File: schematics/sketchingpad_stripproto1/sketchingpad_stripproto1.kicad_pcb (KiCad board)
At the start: 4 copper layers, 160 x 59.6 mm, 73 parts, among them CN1 HC-1.0-4PWT, CN2 S2B-PH-SM4-TB, J1 Conn_01x07, J2 Conn_01x07, J3 Conn_01x03, SW1 TS-1088-AR02016, U1 TS20

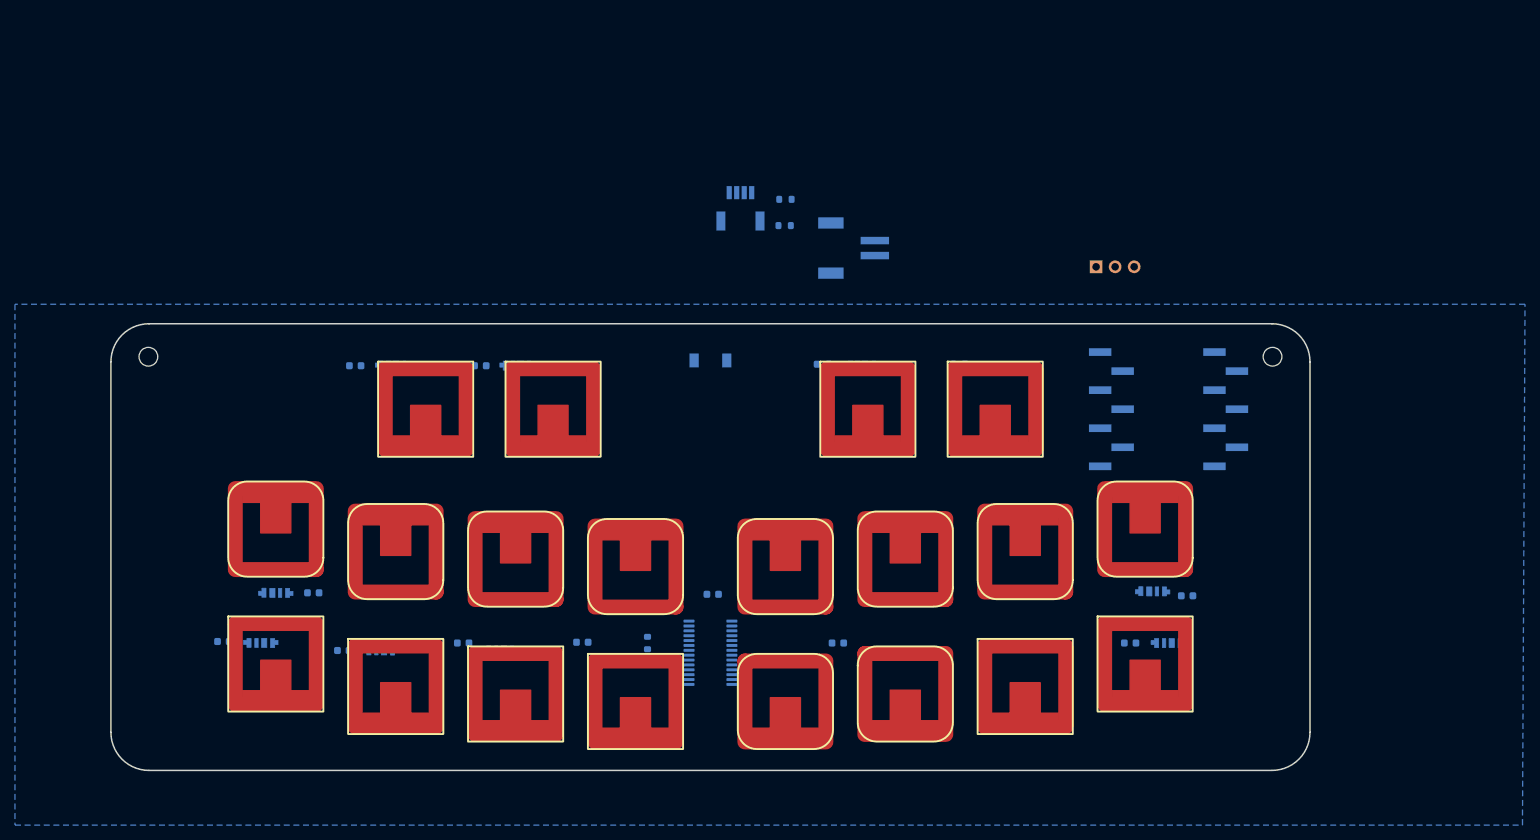
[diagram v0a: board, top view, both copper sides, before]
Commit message: add arduino hwtest
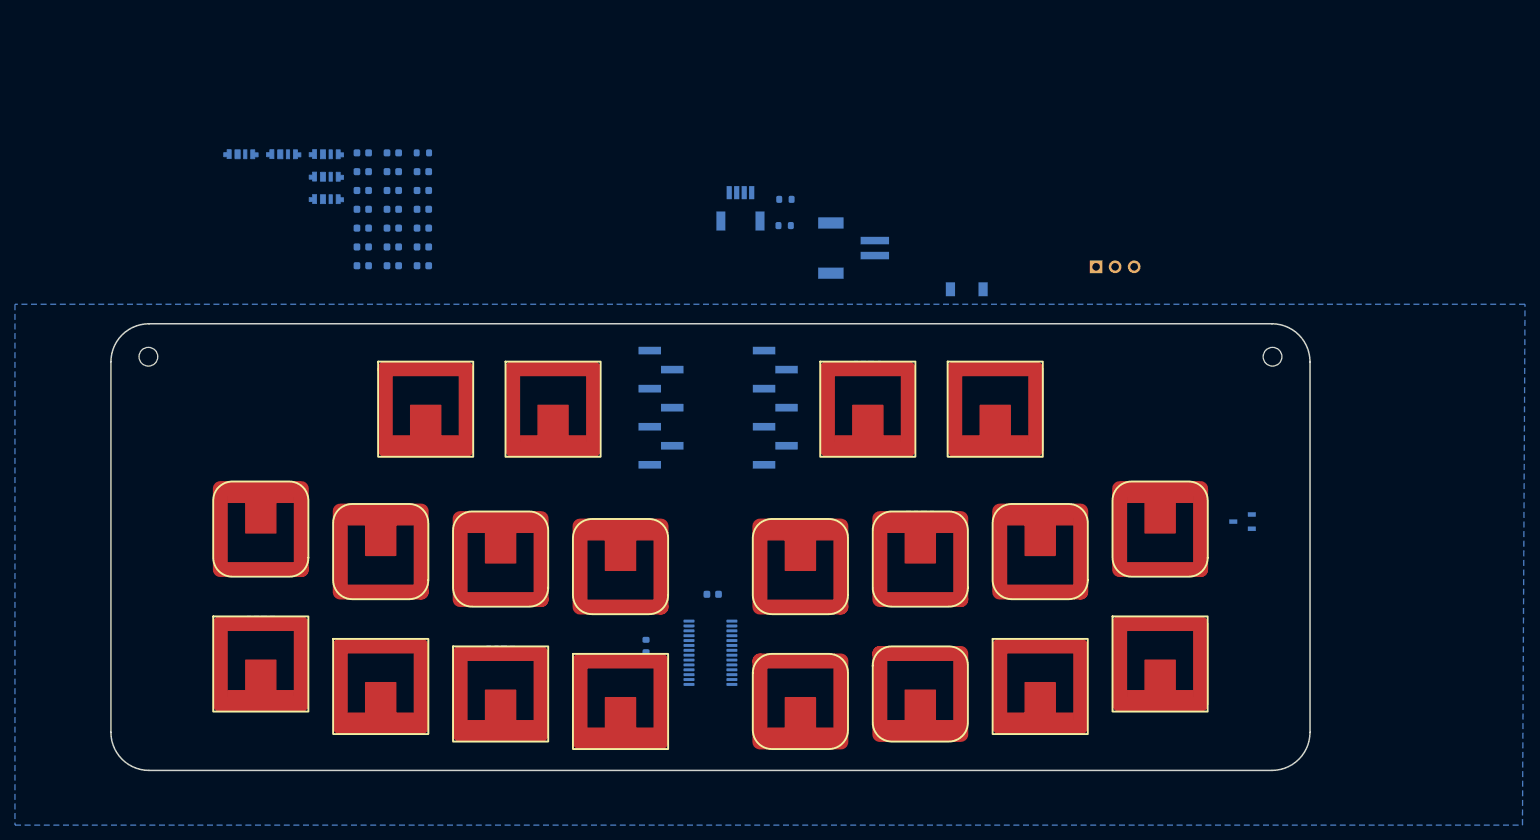
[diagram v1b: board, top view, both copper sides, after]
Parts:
- added Q1: AO3415A, easyeda2kicad:SOT-23-3_L2.9-W1.6-P1.90-LS2.8-BR, B.Cu at (207.0, 122.0)
- added R19: 100k, Resistor_SMD:R_0603_1608Metric, B.Cu at (97.6, 72.8)
- moved LED16 129.9 mm to (84.8, 73.0), turned to 0 degrees
- moved LED8 123.4 mm to (84.8, 76.0)
- moved C8 115.4 mm to (97.6, 77.8), turned to 0 degrees
- moved C16 113.4 mm to (97.6, 75.3)
- moved LED15 112.2 mm to (84.8, 79.0), turned to 0 degrees
- moved C7 98.1 mm to (97.6, 82.8), turned to 0 degrees
- moved C15 96.6 mm to (97.6, 80.3)
- moved LED5 90.1 mm to (79.0, 73.0)
- moved C13 88.3 mm to (93.6, 72.8)
- moved C6 82.1 mm to (97.6, 87.9), turned to 0 degrees
- moved C14 81.7 mm to (97.6, 85.3)
- moved C5 81.2 mm to (93.6, 75.3), turned to 0 degrees
- moved C20 77.7 mm to (93.6, 82.8)
- moved C19 67.6 mm to (89.6, 72.8)
- moved C12 65.4 mm to (93.6, 77.8), turned to 0 degrees
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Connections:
- net /Root/SCL renamed /SCL
- net /Root/SDA renamed /SDA
- net /Root/TOUCH1 renamed /TOUCH1
- net /Root/TOUCH10 renamed /TOUCH10
- net /Root/TOUCH11 renamed /TOUCH11
- net /Root/TOUCH12 renamed /TOUCH12
- net /Root/TOUCH13 renamed /TOUCH13
- net /Root/TOUCH14 renamed /TOUCH14
- net /Root/TOUCH15 renamed /TOUCH15
- net /Root/TOUCH16 renamed /TOUCH16
- net /Root/TOUCH17 renamed /TOUCH17
- net /Root/TOUCH18 renamed /TOUCH18
- net /Root/TOUCH19 renamed /TOUCH19
- net /Root/TOUCH2 renamed /TOUCH2
- net /Root/TOUCH20 renamed /TOUCH20
- net /Root/TOUCH3 renamed /TOUCH3
- net /Root/TOUCH4 renamed /TOUCH4
- net /Root/TOUCH5 renamed /TOUCH5
- net /Root/TOUCH6 renamed /TOUCH6
- net /Root/TOUCH7 renamed /TOUCH7
- net /Root/TOUCH8 renamed /TOUCH8
- net /Root/TOUCH9 renamed /TOUCH9
- net LED_DAT renamed /LED_DAT
- C1 pad 1: +3.3V -> 3V3_LED
- C10 pad 1: +3.3V -> 3V3_LED
- C11 pad 1: +3.3V -> 3V3_LED
- C12 pad 1: +3.3V -> 3V3_LED
- C13 pad 1: +3.3V -> 3V3_LED
- C14 pad 1: +3.3V -> 3V3_LED
- C15 pad 1: +3.3V -> 3V3_LED
- C16 pad 1: +3.3V -> 3V3_LED
- C17 pad 1: +3.3V -> 3V3_LED
- C18 pad 1: +3.3V -> 3V3_LED
- C19 pad 1: +3.3V -> 3V3_LED
- C2 pad 1: +3.3V -> 3V3_LED
- C20 pad 1: +3.3V -> 3V3_LED
- C3 pad 1: +3.3V -> 3V3_LED
- C4 pad 1: +3.3V -> 3V3_LED
- C5 pad 1: +3.3V -> 3V3_LED
- C6 pad 1: +3.3V -> 3V3_LED
- C7 pad 1: +3.3V -> 3V3_LED
- C8 pad 1: +3.3V -> 3V3_LED
- C9 pad 1: +3.3V -> 3V3_LED
- CN2 pad 2: unconnected-(CN2-Pad2) -> /VBAT
- J1 pad 3: unconnected-(J1-Pin_3-Pad3) -> /BUTTON
- J1 pad 4: unconnected-(J1-Pin_4-Pad4) -> /TS20_INT
- J2 pad 7: unconnected-(J2-Pin_7-Pad7) -> /LED_POWER
- J3 pad 1: /Root/VBAT -> /VBAT
- LED1 pad 2: +3.3V -> 3V3_LED
- LED10 pad 2: +3.3V -> 3V3_LED
- LED11 pad 2: +3.3V -> 3V3_LED
- LED12 pad 2: +3.3V -> 3V3_LED
- LED13 pad 2: +3.3V -> 3V3_LED
- LED14 pad 2: +3.3V -> 3V3_LED
- LED15 pad 2: +3.3V -> 3V3_LED
- LED16 pad 2: +3.3V -> 3V3_LED
- LED17 pad 2: +3.3V -> 3V3_LED
- LED18 pad 2: +3.3V -> 3V3_LED
- LED19 pad 2: +3.3V -> 3V3_LED
- LED2 pad 2: +3.3V -> 3V3_LED
- LED20 pad 2: +3.3V -> 3V3_LED
- LED3 pad 2: +3.3V -> 3V3_LED
- LED4 pad 2: +3.3V -> 3V3_LED
- LED5 pad 2: +3.3V -> 3V3_LED
- LED6 pad 2: +3.3V -> 3V3_LED
- LED7 pad 2: +3.3V -> 3V3_LED
- LED8 pad 2: +3.3V -> 3V3_LED
- LED9 pad 2: +3.3V -> 3V3_LED
- R16 pad 1: Net-(U1-INT) -> /TS20_INT
- SW1 pad 1: unconnected-(SW1-Pad1) -> /BUTTON
- U1 pad 19: Net-(U1-INT) -> /TS20_INT

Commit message: going with SMD-mounted XIAO I guess, added audio. ERC clean
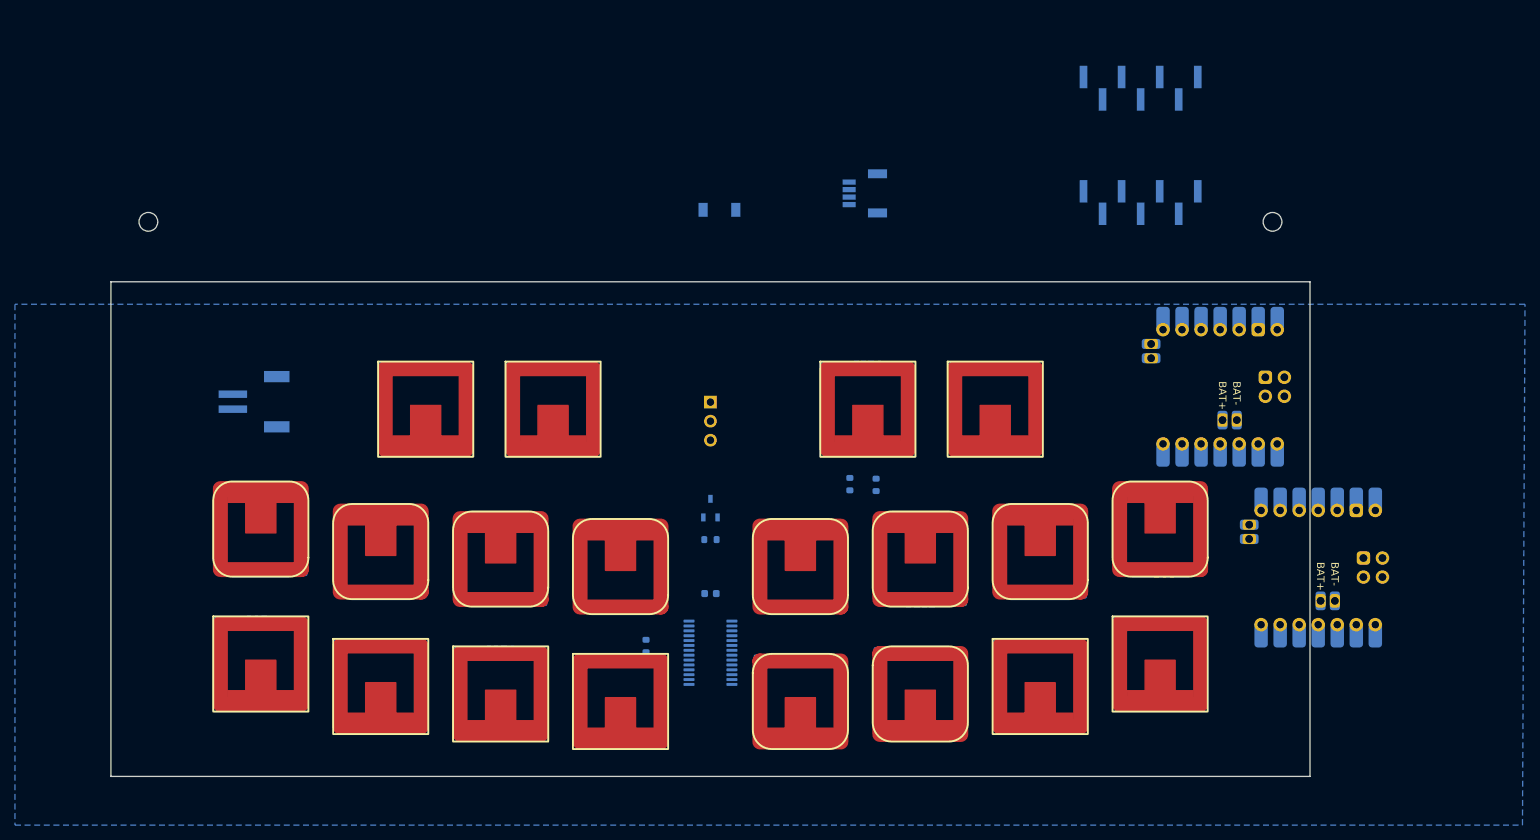
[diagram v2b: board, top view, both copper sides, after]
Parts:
- added U2: Seeeduino Xiao nRF52840, PCM_marbastlib-xp-promicroish:Xiao_nRF52840_ACH, B.Cu at (204.0, 104.0)
- added U3: XIAO-nRF52840-SMD, PCM_marbastlib-xp-promicroish:Xiao_nRF52840_ACH, B.Cu at (217.1, 128.1)
- moved LED16 127.5 mm to (196.0, 135.3), turned to 180 degrees
- moved LED8 123.2 mm to (196.0, 128.8)
- moved C8 115.1 mm to (200.8, 128.8), turned to 180 degrees
- moved LED15 112.2 mm to (180.0, 138.2), turned to 180 degrees
- moved C16 110.9 mm to (191.0, 135.2)
- moved C7 100.2 mm to (185.0, 131.8), turned to 180 degrees
- moved C15 96.6 mm to (175.0, 138.2)
- moved LED5 91.9 mm to (148.0, 133.8)
- moved C6 84.3 mm to (169.0, 132.8), turned to 180 degrees
- moved C13 83.6 mm to (143.0, 140.2)
- moved C5 83.2 mm to (152.8, 133.8), turned to 180 degrees
- moved CN2 82.4 mm to (75.2, 106.0), turned to -90 degrees
- moved C14 81.7 mm to (159.0, 139.2)
- moved C20 77.6 mm to (169.0, 101.2)
- moved J2 76.9 mm to (193.4, 64.2), turned to 180 degrees
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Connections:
- J1 pad 1: unconnected-(J1-Pin_1-Pad1) -> /PWM_AUDIO
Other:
- board size 160 x 59.6 mm -> 160 x 66 mm

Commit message: final on the sketchingpad_stripproto1 sch maybe
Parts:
- removed J1, J2: Conn_01x07, easyeda2kicad:HDR-SMD_7P-P2.54_HX-PM2.54-1X7P-TP-YQ
- removed U3: XIAO-nRF52840-SMD, PCM_marbastlib-xp-promicroish:Xiao_nRF52840_ACH
- added C21: 100n, Capacitor_SMD:C_0603_1608Metric, B.Cu at (77.5, 75.7)
- added C22: 47u, Capacitor_SMD:C_0603_1608Metric, B.Cu at (80.0, 75.7)
- added R21: 220, Resistor_SMD:R_0603_1608Metric, B.Cu at (82.5, 75.7)
- added R22: 100, Resistor_SMD:R_0603_1608Metric, B.Cu at (85.0, 75.7)
- added R23: 1.8k, Resistor_SMD:R_0603_1608Metric, B.Cu at (87.5, 75.7)
- added SW2: MINI MSK12CO2, easyeda2kicad:SW-SMD_MSK12CO2, B.Cu at (188.8, 62.3)
- added TP21: TestPoint, TestPoint:TestPoint_Pad_D1.5mm, B.Cu at (197.4, 76.3)
- added TP22: TestPoint, TestPoint:TestPoint_Pad_D1.5mm, B.Cu at (200.9, 76.3)
- J3: value Conn_01x03 -> AudioJack4; footprint Connector_PinSocket_2.54mm:PinSocket_1x03_P2.54mm_Vertical -> todbot_stuff:Jack_3.5mm_PJ320D_Horizontal
- SW1: value TS-1088-AR02016 -> TC-S3601-3.5-260G-F0.6; footprint easyeda2kicad:SW-SMD_L3.9-W3.0-P4.45 -> easyeda2kicad:SW-SMD_TC-S3601-3.5-260G-F0.6
- U2: footprint PCM_marbastlib-xp-promicroish:Xiao_nRF52840_ACH -> todbot_stuff:Xiao_nRF52840_ACH-todedit
- moved CN2 129.5 mm to (199.0, 68.0), turned to 180 degrees
- moved U2 75.7 mm to (136.0, 70.7), turned to 180 degrees
- moved J3 68.0 mm to (80.2, 67.2), turned to -90 degrees
- moved R19 41.6 mm to (128.5, 83.5)
- moved SW1 35.8 mm to (106.4, 62.1), turned to 180 degrees
- moved Q1 34.1 mm to (128.4, 87.0), turned to 90 degrees
- moved C1 31.0 mm to (81.0, 97.8)
- moved C2 31.0 mm to (96.8, 100.8)
- moved C3 31.0 mm to (113.0, 101.8)
- moved C4 31.0 mm to (128.8, 102.8)
- moved C5 31.0 mm to (152.8, 102.8)
- moved C6 31.0 mm to (169.0, 101.8)
- moved C7 31.0 mm to (185.0, 100.8)
- moved C8 31.0 mm to (200.8, 97.8)
- moved LED1 31.0 mm to (76.0, 97.7)
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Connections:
- CN2 pad 2: /VBAT -> Net-(CN2-Pad2)
- LED1 pad 1: /LED_DAT -> /LED_DATA
- U2 pad 1: unconnected-(U2-P0.02-Pad1) -> /PWM_AUDIO
- U2 pad 10: unconnected-(U2-3V3-Pad10) -> +3.3V
- U2 pad 11: unconnected-(U2-P1.15-Pad11) -> /BUTTON
- U2 pad 14: unconnected-(U2-P1.12-Pad14) -> /LED_POWER
- U2 pad 15: unconnected-(U2-BAT--Pad15) -> GND
- U2 pad 16: unconnected-(U2-BAT+-Pad16) -> /VBAT
- U2 pad 4: unconnected-(U2-P0.29-Pad4) -> /TS20_INT
- U2 pad 5: unconnected-(U2-P0.04-Pad5) -> /SDA
- U2 pad 6: unconnected-(U2-P0.05-Pad6) -> /SCL
- U2 pad 7: unconnected-(U2-P1.11-Pad7) -> /LED_DATA
- U2 pad 9: unconnected-(U2-GND-Pad9) -> GND
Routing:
- net /VBAT: track 0.00 -> 63.6 mm, vias 0 -> 1
- net /PWM_AUDIO: track 0.00 -> 63.6 mm
- net /SDA: track 0.00 -> 45.8 mm, vias 0 -> 2
- net /TS20_INT: track 0.00 -> 45.5 mm, vias 0 -> 1
- net /SCL: track 0.00 -> 45.0 mm, vias 0 -> 2
- net /BUTTON: track 0.00 -> 24.2 mm, vias 0 -> 1
- net Net-(CN2-Pad2): track 0.00 -> 20.5 mm
- net GND: track 0.00 -> 14.0 mm
- net /LED_POWER: track 0.00 -> 7.83 mm
- net +3.3V: track 0.00 -> 2.27 mm
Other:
- board size 160 x 66 mm -> 158.5 x 66 mm
- board text added: "+"
- board text added: "-"
- board text added: "-+dc"
- board text added: "BAT"
- board text added: "BLKWIRE!"
- board text added: "REDWIRE!"
- board text added: "audio"
- board text added: "leddat"
- board text added: "ledpwr"
- board text removed: "3v3 - Vbat"
- board text removed: "LED_DAT"
- board text removed: "QTPY/XIAO"
- board text removed: "cd+-"

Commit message: more routed
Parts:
- removed C100: 100n, Capacitor_SMD:C_0603_1608Metric
- removed R16, R17, R18: 10k, Resistor_SMD:R_0603_1608Metric
- removed R19: 100k, Resistor_SMD:R_0603_1608Metric
- removed R21: 220, Resistor_SMD:R_0603_1608Metric
- removed R22: 100, Resistor_SMD:R_0603_1608Metric
- removed R23: 1.8k, Resistor_SMD:R_0603_1608Metric
- added C23: 100n, Capacitor_SMD:C_0603_1608Metric, B.Cu at (136.0, 101.8)
- added R1: 10k, Resistor_SMD:R_0603_1608Metric, B.Cu at (136.0, 99.8)
- added R2: 10k, Resistor_SMD:R_0603_1608Metric, B.Cu at (136.0, 97.8)
- added R3: 10k, Resistor_SMD:R_0603_1608Metric, B.Cu at (136.0, 95.8)
- added R4: 100k, Resistor_SMD:R_0603_1608Metric, B.Cu at (70.7, 71.5)
- added R5: 220, Resistor_SMD:R_0603_1608Metric, B.Cu at (70.7, 69.0)
- added R6: 100, Resistor_SMD:R_0603_1608Metric, B.Cu at (70.7, 66.5)
- added R7: 1.8k, Resistor_SMD:R_0603_1608Metric, B.Cu at (70.7, 64.0)
- LED1, LED10, LED11, LED12, LED13, LED14, LED15, LED16, LED17, LED18, LED19, LED2, LED20, LED3, LED4, LED5, LED6, LED7, LED8, LED9: footprint easyeda2kicad:LED-SMD_4P-L4.0-W1.6-L -> todbot_stuff:LED-SMD_4P-L4.0-W1.6-L-todedits
- moved C3 15.3 mm to (103.0, 90.2), turned to 0 degrees
- moved C1 15.2 mm to (71.2, 86.2), turned to 0 degrees
- moved C2 15.2 mm to (87.0, 89.2), turned to 0 degrees
- moved C4 15.0 mm to (119.0, 91.4), turned to 0 degrees
- moved LED2 11.6 mm to (92.0, 89.2), turned to 180 degrees
- moved LED5 11.6 mm to (148.0, 91.2), turned to 180 degrees
- moved LED6 11.6 mm to (164.0, 90.2), turned to 180 degrees
- moved LED8 11.6 mm to (196.0, 86.2), turned to 180 degrees
- moved LED1 11.5 mm to (76.0, 86.2), turned to 180 degrees
- moved LED3 11.5 mm to (108.0, 90.2), turned to 180 degrees
- moved LED4 11.5 mm to (124.0, 91.2), turned to 180 degrees
- moved LED7 11.5 mm to (180.0, 89.2), turned to 180 degrees
- moved C13 9.60 mm to (152.6, 109.0)
- moved Q1 2.00 mm to (128.4, 85.0)
- moved CN2 1.00 mm to (199.0, 67.0)
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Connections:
- U1 pad 1: /TOUCH4 -> /TOUCH17
- U1 pad 11: /TOUCH19 -> /TOUCH13
- U1 pad 12: /TOUCH18 -> /TOUCH14
- U1 pad 13: /TOUCH17 -> /TOUCH15
- U1 pad 15: /TOUCH15 -> /TOUCH9
- U1 pad 16: /TOUCH11 -> /TOUCH10
- U1 pad 17: /TOUCH1 -> /TOUCH11
- U1 pad 18: /TOUCH7 -> /TOUCH12
- U1 pad 2: /TOUCH9 -> /TOUCH18
- U1 pad 25: /TOUCH12 -> /TOUCH1
- U1 pad 27: /TOUCH8 -> /TOUCH3
- U1 pad 28: /TOUCH3 -> /TOUCH4
- U1 pad 3: /TOUCH5 -> /TOUCH19
- U1 pad 6: /TOUCH10 -> /TOUCH5
- U1 pad 8: /TOUCH13 -> /TOUCH7
- U1 pad 9: /TOUCH14 -> /TOUCH8
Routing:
- net /TOUCH9: track 0.00 -> 75.8 mm, vias 0 -> 1
- net /TOUCH16: track 0.00 -> 75.1 mm, vias 0 -> 1
- net /TOUCH1: track 0.00 -> 65.8 mm, vias 0 -> 1
- net /TOUCH8: track 0.00 -> 65.3 mm, vias 0 -> 1
- net /TOUCH17: track 0.00 -> 57.8 mm, vias 0 -> 1
- net /TOUCH15: track 0.00 -> 56.8 mm, vias 0 -> 1
- net /TOUCH10: track 0.00 -> 56.2 mm, vias 0 -> 1
- net /TOUCH20: track 0.00 -> 55.1 mm, vias 0 -> 1
- net +3.3V: track 2.27 -> 54.7 mm, vias 0 -> 2
- net /TOUCH7: track 0.00 -> 47.7 mm, vias 0 -> 1
- net /TOUCH2: track 0.00 -> 47.0 mm, vias 0 -> 1
- net /TOUCH18: track 0.00 -> 43.7 mm, vias 0 -> 1
- net /TOUCH14: track 0.00 -> 39.8 mm, vias 0 -> 1
- net /TOUCH11: track 0.00 -> 39.0 mm, vias 0 -> 1
- net /TOUCH19: track 0.00 -> 38.3 mm, vias 0 -> 1
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
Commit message: more routed
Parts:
- added 3V3_LED: 3V3_LED, TestPoint:TestPoint_Pad_D1.5mm, B.Cu at (64.6, 80.2)
- moved R4 62.7 mm to (131.6, 86.2)
- moved C7 11.6 mm to (184.9, 89.2), turned to 0 degrees
- moved C8 11.6 mm to (200.9, 86.2), turned to 0 degrees
- moved C5 11.6 mm to (152.8, 91.2), turned to 0 degrees
- moved C6 11.4 mm to (168.9, 90.4), turned to 0 degrees
- moved Q1 1.08 mm to (129.4, 84.6)
- moved C4 0.40 mm to (119.0, 91.0)
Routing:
- net 3V3_LED: track 19.6 -> 499.7 mm, vias 2 -> 43
- net Net-(LED16-DOUT): track 0.00 -> 165.4 mm, vias 0 -> 2
- net Net-(LED8-DOUT): track 0.00 -> 160.0 mm, vias 0 -> 2
- net /LED_DATA: track 0.00 -> 96.9 mm
- net Net-(LED18-DOUT): track 0.00 -> 73.6 mm, vias 0 -> 2
- net Net-(LED12-DOUT): track 0.00 -> 30.6 mm, vias 0 -> 2
- net Net-(LED4-DOUT): track 0.00 -> 30.5 mm, vias 0 -> 2
- net Net-(LED1-DOUT): track 0.00 -> 25.3 mm
- net Net-(LED10-DIN): track 0.00 -> 23.7 mm
- net Net-(LED6-DOUT): track 0.00 -> 23.4 mm
- net Net-(LED3-DOUT): track 0.00 -> 23.3 mm
- net Net-(LED14-DOUT): track 0.00 -> 22.9 mm
- net Net-(LED10-DOUT): track 0.00 -> 22.9 mm
- net Net-(LED5-DOUT): track 0.00 -> 22.7 mm
- net Net-(LED2-DOUT): track 0.00 -> 22.6 mm
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
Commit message: 0 unrouted. DRC is a mess tho
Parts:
- moved R5 15.5 mm to (84.6, 75.8), turned to 90 degrees
- moved R6 12.3 mm to (78.8, 75.8), turned to -90 degrees
- moved R7 11.9 mm to (72.4, 75.8), turned to 90 degrees
- moved C22 4.21 mm to (75.8, 75.8)
- moved C21 4.10 mm to (81.6, 75.8), turned to 90 degrees
- moved R4 3.44 mm to (129.6, 83.4)
- moved Q1 1.61 mm to (129.6, 86.2)
- moved CN1 0.80 mm to (136.0, 88.8)
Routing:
- net Net-(C22-Pad1): track 0.00 -> 13.5 mm
- net Net-(C21-Pad1): track 0.00 -> 8.86 mm
- net +3.3V: track 59.2 -> 64.6 mm, vias 3 -> 4
- net /PWM_AUDIO: track 63.6 -> 68.5 mm
- net /SCL: track 42.5 -> 45.6 mm
- net Net-(LED8-DOUT): track 160.0 -> 162.2 mm
- net /SDA: track 44.6 -> 46.3 mm
- net /LED_POWER: track 5.07 -> 6.75 mm
- net 3V3_LED: track 499.7 -> 501.1 mm
- net /LED_DATA: track 96.9 -> 96.6 mm, vias 0 -> 2

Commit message: DRC better
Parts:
- moved SW2 0.05 mm to (188.8, 62.4)
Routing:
- net 3V3_LED: vias 43 -> 42
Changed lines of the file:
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@@
 	(footprint "easyeda2kicad:SW-SMD_MSK12CO2"
 		(layer "B.Cu")
-		(at 188.795 62.3)
+		(at 188.795 62.35)
 		(property "Reference" "SW2"
 			(at 4.705 -0.3 180)
@@
 	(footprint "easyeda2kicad:SW-SMD_TC-S3601-3.5-260G-F0.6"
 		(layer "B.Cu")
-		(at 106.400051 62.0625 180)
+		(at 106.400051 62.1125 180)
 		(property "Reference" "SW1"
 			(at 0.000051 -2.5375 0)
@@
 		(size 0.5)
 		(drill 0.3)
-		(layers "F.Cu" "B.Cu")
-		(net "3V3_LED")
-	)
-	(via
-		(at 98.4 69.6)
-		(size 0.5)
-		(drill 0.3)

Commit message: ERC and DRC pass
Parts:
- renumbered J3 to J1, 3V3_LED to TP23
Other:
- board text added: "3v3_led"
- board text added: "BLK WIRE!"
- board text added: "RED WIRE!"
- board text removed: "BLKWIRE!"
- board text removed: "REDWIRE!"
